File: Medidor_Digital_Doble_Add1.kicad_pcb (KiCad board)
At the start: 2 copper layers, 21 x 21.7 mm, 12 parts, among them J1 Screw_Terminal_01x01, J2 Screw_Terminal_01x01, J3 Screw_Terminal_01x01, J4 Screw_Terminal_01x01, J5 Screw_Terminal_01x01, J6 Screw_Terminal_01x01, U1 INA823

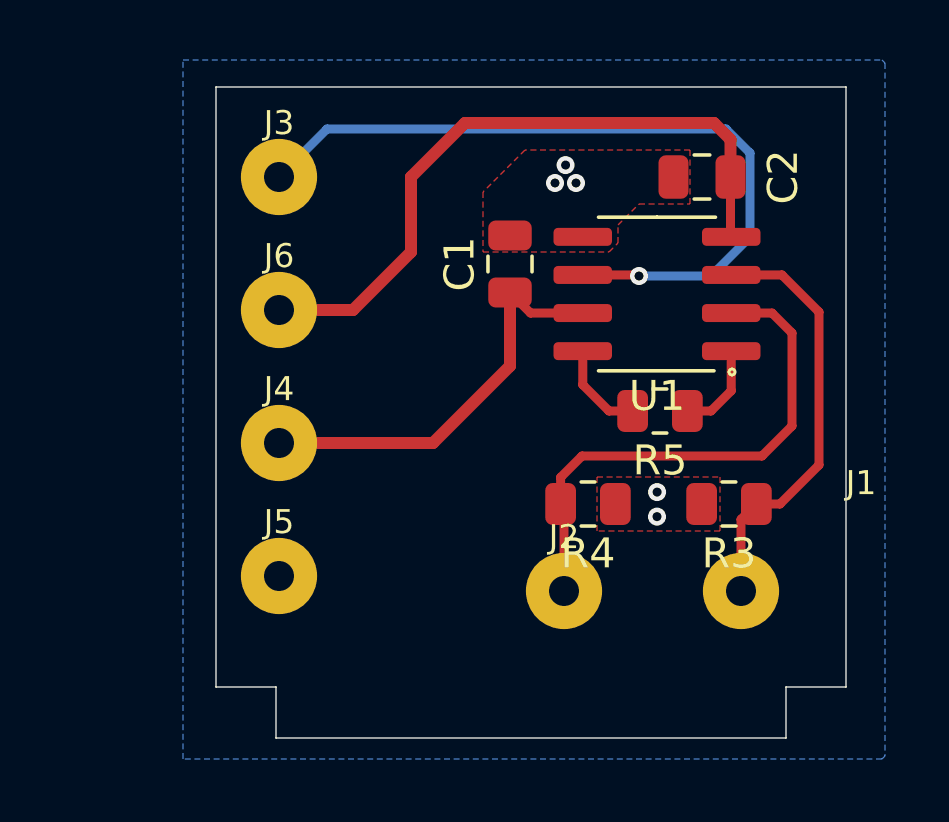
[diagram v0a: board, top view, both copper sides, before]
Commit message: SCH:Se cambia la resistencia de 1.2k a 1k. PCB:Se rediseña la distribución para menor altura de la placa.
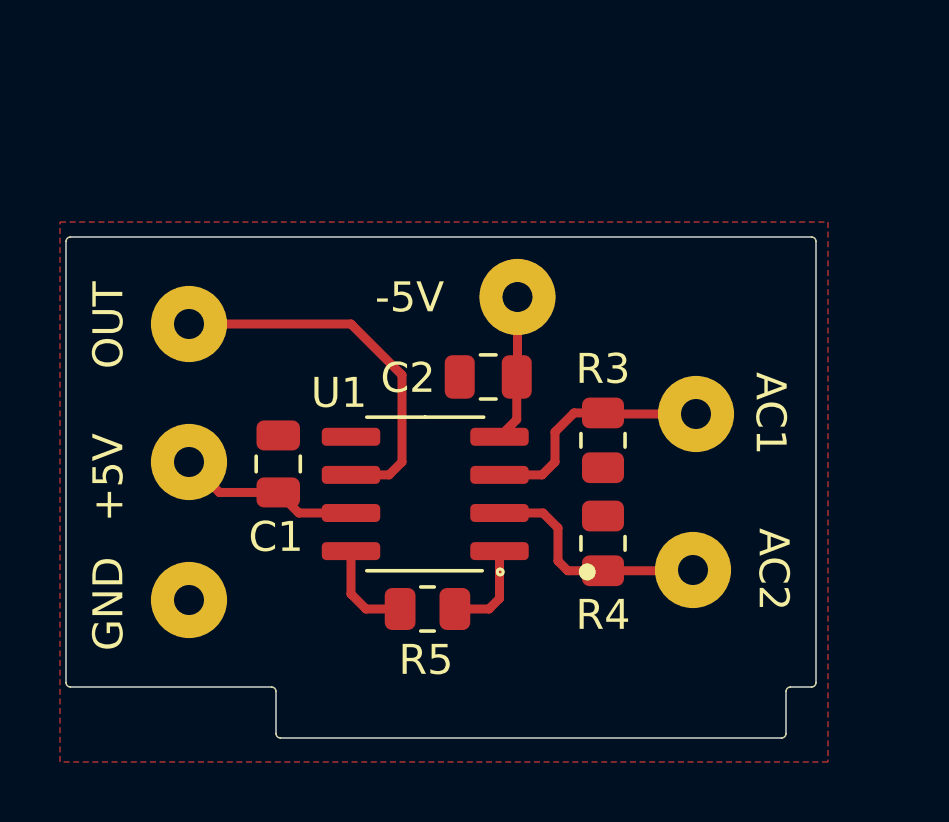
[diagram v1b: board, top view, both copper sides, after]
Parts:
- R3, R4: value 1k2 -> 1k
- moved C1 10.2 mm to (121.4, 111.7)
- moved U1 10.2 mm to (126.3, 112.7)
- moved R5 10.2 mm to (126.3, 116.5)
- moved C2 9.76 mm to (128.4, 108.8)
- moved J6 7.96 mm to (129.3, 106.1)
- moved J1 6.09 mm to (135.3, 110.0)
- moved J3 5.75 mm to (118.4, 107.0)
- moved R3 4.71 mm to (132.2, 110.9), turned to -90 degrees
- moved J2 4.36 mm to (135.2, 115.2)
- moved J5 3.10 mm to (118.4, 116.2)
- moved J4 3.07 mm to (118.4, 111.6)
- moved R4 1.40 mm to (132.2, 114.3), turned to -90 degrees
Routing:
- net -5V: track 22.6 -> 4.91 mm
- net V1: track 25.6 -> 12.6 mm, vias 1 -> 0
- net AC2: track 17.7 -> 7.90 mm
- net +5V: track 13.9 -> 6.10 mm
- net AC1: track 14.3 -> 8.01 mm
- net GND: vias 5 -> 0
- removed copper zone on B.Cu, net GND
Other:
- board size 21 x 21.7 mm -> 25 x 16.7 mm
- board text added: "+5V"
- board text added: "-5V"
- board text added: "AC1"
- board text added: "AC2"
- board text added: "GND"
- board text added: "OUT"
